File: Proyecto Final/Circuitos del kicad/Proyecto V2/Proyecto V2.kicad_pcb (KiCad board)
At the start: 2 copper layers, 249.8 x 175.1 mm, 40 parts, among them J1 12v, J2 I2C + LCD, J3 DS1307, J4 Encoder, J5 Conn_01x02, J6 Conn_01x02, J7 Conn_01x02, J8 Conn_01x05, J9 Conn_01x05, K1 RAYEX-L90, K2 RAYEX-L90, K3 RAYEX-L90, Q1 PN2222A, Q2 PN2222A, Q3 PN2222A, SW1 SW_Push, SW2 SW_Push, SW3 SW_Push, SW4 SW_Push, U1 LM7805, U3 ATmega328P-P, U4 NodeMCU1.0(ESP-12E), Y1 16MHz

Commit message: SEXOOO
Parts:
- removed J9: Conn_01x05, Connector_PinHeader_2.54mm:PinHeader_1x05_P2.54mm_Vertical
- J4: value Encoder -> Conn_02x06_Odd_Even; footprint Connector_PinSocket_2.54mm:PinSocket_1x05_P2.54mm_Vertical -> Connector_PinHeader_2.54mm:PinHeader_2x06_P2.54mm_Vertical; moved to B.Cu
- moved J4 21.3 mm to (70.3, 44.4)
- moved C2 17.3 mm to (35.6, 64.7)
- moved RELAY1 17.3 mm to (66.6, 79.0)
- moved C1 17.3 mm to (35.6, 47.1)
- moved C3 17.3 mm to (56.6, 81.7)
- moved C4 17.3 mm to (41.5, 81.6)
- moved DS18B20 17.3 mm to (55.3, 70.6)
- moved J1 17.3 mm to (46.5, 88.3)
- moved J2 17.3 mm to (66.5, 30.3)
- moved J3 17.3 mm to (61.7, 30.3)
- moved Lvl_sens1 17.3 mm to (56.9, 43.7)
- moved R1 17.3 mm to (60.4, 66.7)
- moved U1 17.3 mm to (51.6, 75.9)
- moved U3 17.3 mm to (45.2, 33.6)
- moved Y1 17.3 mm to (38.4, 53.4)
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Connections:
- J4 pad 1: Net-(J4-Pad1) -> +5V
- J4 pad 2: Net-(J4-Pad2) -> +5V
- J4 pad 3: unconnected-(J4-Pad3) -> Net-(U3-Pad4)
- J4 pad 4: +5V -> Net-(J4-Pad4)
- J4 pad 5: GND -> Net-(U3-Pad5)
- U3 pad 23: Net-(J4-Pad1) -> Net-(J4-Pad8)
- U3 pad 24: Net-(J4-Pad2) -> Net-(J4-Pad6)
- U3 pad 25: unconnected-(U3-Pad25) -> Net-(J4-Pad4)
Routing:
- net Net-(U3-Pad11): track 31.9 -> 136.1 mm
- net Net-(U3-Pad6): track 17.0 -> 99.6 mm
- net Net-(U3-Pad5): track 16.1 -> 87.8 mm
- net Net-(U3-Pad4): track 16.1 -> 77.3 mm
- net +12V: track 424.7 -> 399.3 mm
- net Net-(J4-Pad4): track 0.00 -> 18.0 mm
- net Net-(J4-Pad6): track 0.00 -> 17.8 mm
- net Net-(J4-Pad8): track 0.00 -> 17.6 mm
- net +5V: track 182.4 -> 165.7 mm
- net Net-(D3-Pad2): track 41.8 -> 30.5 mm
- net Net-(J4-Pad2): track 11.1 -> 0.00 mm
- net Net-(J4-Pad1): track 11.1 -> 0.00 mm
- net Net-(D2-Pad2): track 39.1 -> 34.2 mm
- net GND: track 445.5 -> 441.8 mm
- net Net-(D1-Pad2): track 48.9 -> 52.0 mm
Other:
- board size 249.8 x 175.1 mm -> 239.5 x 178.8 mm

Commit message: Resistencias pullup para pulsadores
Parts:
- removed J8: Conn_01x05, Connector_PinHeader_2.54mm:PinHeader_1x05_P2.54mm_Vertical
- added Encoder/puls1: Conn_02x06_Odd_Even, Connector_PinHeader_2.54mm:PinHeader_2x06_P2.54mm_Vertical, F.Cu at (223.7, 47.6)
- added Encoder1: Conn_01x05, Connector_PinSocket_2.54mm:PinSocket_1x05_P2.54mm_Vertical, F.Cu at (212.9, 19.8)
- added R5: 10k, Resistor_THT:R_Axial_DIN0204_L3.6mm_D1.6mm_P5.08mm_Horizontal, F.Cu at (222.0, 31.8)
- added R6: 10k, Resistor_THT:R_Axial_DIN0204_L3.6mm_D1.6mm_P5.08mm_Horizontal, F.Cu at (218.9, 31.8)
- added R7: 10k, Resistor_THT:R_Axial_DIN0204_L3.6mm_D1.6mm_P5.08mm_Horizontal, F.Cu at (216.0, 31.8)
- added R8: 10k, Resistor_THT:R_Axial_DIN0204_L3.6mm_D1.6mm_P5.08mm_Horizontal, F.Cu at (212.8, 31.8)
- moved SW1 42.1 mm to (174.0, 21.7), turned to 0 degrees
- moved SW2 37.3 mm to (192.4, 21.7), turned to 0 degrees
- moved SW3 14.9 mm to (230.8, 21.8), turned to 0 degrees
- moved SW4 12.1 mm to (248.7, 21.8), turned to 0 degrees
- renumbered ESP2866 to ESP2866-arduino1, U4 to ESP8266, J4 to Encoder/puls-arduino1, K1 to Relay-1, K3 to Relay-2, K2 to Relay-3, J5 to Salida-1, J7 to Salida-2, J6 to Salida-3
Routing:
- net +5V: track 165.7 -> 370.6 mm
- net Net-(Encoder/puls1-Pad4): track 0.00 -> 131.7 mm
- net Net-(Encoder/puls1-Pad6): track 0.00 -> 121.8 mm
- net Net-(Encoder/puls1-Pad8): track 0.00 -> 111.7 mm
- net GND: track 441.8 -> 486.6 mm
- net Net-(Encoder/puls1-Pad9): track 30.4 -> 46.5 mm
- net Net-(Encoder/puls1-Pad3): track 33.8 -> 46.1 mm
- net Net-(Encoder/puls-arduino1-Pad9): track 136.1 -> 126.6 mm
- net Net-(Encoder/puls1-Pad7): track 25.2 -> 33.2 mm
- net Net-(U3-Pad6): track 99.6 -> 92.4 mm
- net Net-(Encoder/puls-arduino1-Pad5): track 87.8 -> 83.6 mm
- net Net-(Encoder/puls1-Pad5): track 29.4 -> 32.0 mm
- net Net-(Encoder/puls-arduino1-Pad3): track 77.3 -> 75.7 mm
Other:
- board size 239.5 x 178.8 mm -> 238.9 x 178.8 mm

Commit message: Cambio GND
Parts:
- moved SW1 14.2 mm to (159.8, 21.7)
- moved SW2 14.2 mm to (178.2, 21.7)
- moved SW4 13.0 mm to (261.7, 21.8)
- moved SW3 13.0 mm to (243.8, 21.8)
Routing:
- net GND: track 486.6 -> 3.69 mm
- net Net-(Encoder/puls1-Pad4): track 131.7 -> 165.2 mm
- net Net-(Encoder/puls1-Pad6): track 121.8 -> 155.1 mm
- net Net-(Encoder/puls1-Pad8): track 111.7 -> 144.6 mm
- net +5V: track 370.6 -> 401.5 mm
- net Net-(Encoder/puls1-Pad5): track 32.0 -> 45.0 mm
- net Net-(Encoder/puls1-Pad7): track 33.2 -> 46.2 mm
- net Net-(Encoder/puls1-Pad9): track 46.5 -> 59.4 mm
- net Net-(Encoder/puls1-Pad3): track 46.1 -> 58.4 mm
- net Net-(Encoder/puls-arduino1-Pad9): track 126.6 -> 127.8 mm
- net Net-(U3-Pad6): track 92.4 -> 93.2 mm
- net Net-(RELAY1-Pad4): track 23.7 -> 23.1 mm
- added copper zone on B.Cu, net GND
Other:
- board size 238.9 x 178.8 mm -> 252.7 x 178.8 mm

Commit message: Detalles menores
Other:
- board size 252.7 x 178.8 mm -> 252.9 x 178.9 mm
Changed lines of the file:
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@@
     (fp_line (start -3.2 9.01) (end 14.48 9.01) (layer "F.SilkS") (width 0.12))
     (fp_line (start 4.064 -5.1054) (end 5.334 -5.1054) (layer "F.SilkS") (width 0.12))
-    (fp_arc (start 5.842266 0.761644) (mid 4.699001 0.381219) (end 5.842001 -0.000002) (layer "F.SilkS") (width 0.12))
+    (fp_arc (start 5.842266 0.761644) (mid 4.699001 0.381223) (end 5.842001 -0.000002) (layer "F.SilkS") (width 0.12))
     (fp_arc (start 10.13 -12.44) (mid 10.384817 -13.055183) (end 11 -13.31) (layer "F.SilkS") (width 0.12))
     (fp_arc (start 5.8418 -0.761733) (mid 4.765964 -0.859168) (end 5.334 -1.778) (layer "F.SilkS") (width 0.12))
@@
     (fp_arc (start 16 14.31) (mid 15.384817 14.055183) (end 15.13 13.44) (layer "F.SilkS") (width 0.12))
     (fp_arc (start 27.08 -13.31) (mid 27.695183 -13.055183) (end 27.95 -12.44) (layer "F.SilkS") (width 0.12))
-    (fp_arc (start 5.334002 1.777997) (mid 4.765969 0.859167) (end 5.841802 0.76173) (layer "F.SilkS") (width 0.12))
-    (fp_arc (start 5.842265 -0.000355) (mid 4.699 -0.38078) (end 5.842 -0.762001) (layer "F.SilkS") (width 0.12))
+    (fp_arc (start 5.334002 1.777997) (mid 4.765966 0.859171) (end 5.841802 0.76173) (layer "F.SilkS") (width 0.12))
+    (fp_arc (start 5.842265 -0.000355) (mid 4.699001 -0.380778) (end 5.842 -0.762001) (layer "F.SilkS") (width 0.12))
     (fp_arc (start 27.95 13.44) (mid 27.695183 14.055183) (end 27.08 14.31) (layer "F.SilkS") (width 0.12))
     (fp_circle (center 21.59 -2.54) (end 21.59 -2.413) (layer "F.SilkS") (width 0.12) (fill none))
@@
     (fp_line (start 17.74 6.604) (end 17.74 1.778) (layer "F.SilkS") (width 0.12))
     (fp_arc (start 5.8418 -0.761733) (mid 4.765964 -0.859168) (end 5.334 -1.778) (layer "F.SilkS") (width 0.12))
-    (fp_arc (start 5.842265 -0.000355) (mid 4.699 -0.38078) (end 5.842 -0.762001) (layer "F.SilkS") (width 0.12))
-    (fp_arc (start 5.842266 0.761644) (mid 4.699001 0.381219) (end 5.842001 -0.000002) (layer "F.SilkS") (width 0.12))
+    (fp_arc (start 5.842265 -0.000355) (mid 4.699001 -0.380778) (end 5.842 -0.762001) (layer "F.SilkS") (width 0.12))
+    (fp_arc (start 5.842266 0.761644) (mid 4.699001 0.381223) (end 5.842001 -0.000002) (layer "F.SilkS") (width 0.12))
     (fp_arc (start 27.08 -13.31) (mid 27.695183 -13.055183) (end 27.95 -12.44) (layer "F.SilkS") (width 0.12))
     (fp_arc (start 16 14.31) (mid 15.384817 14.055183) (end 15.13 13.44) (layer "F.SilkS") (width 0.12))
@@
     (fp_arc (start -4.07 -9.94) (mid -3.815183 -10.555183) (end -3.2 -10.81) (layer "F.SilkS") (width 0.12))
     (fp_arc (start 10.13 -11.46) (mid 9.939619 -11.000381) (end 9.48 -10.81) (layer "F.SilkS") (width 0.12))
-    (fp_arc (start 5.334002 1.777997) (mid 4.765969 0.859167) (end 5.841802 0.76173) (layer "F.SilkS") (width 0.12))
+    (fp_arc (start 5.334002 1.777997) (mid 4.765966 0.859171) (end 5.841802 0.76173) (layer "F.SilkS") (width 0.12))
     (fp_arc (start -3.2 9.01) (mid -3.815183 8.755183) (end -4.07 8.14) (layer "F.SilkS") (width 0.12))
     (fp_arc (start 10.13 -12.44) (mid 10.384817 -13.055183) (end 11 -13.31) (layer "F.SilkS") (width 0.12))
@@
     (fp_arc (start 5.8418 -0.761733) (mid 4.765964 -0.859168) (end 5.334 -1.778) (layer "F.SilkS") (width 0.12))
     (fp_arc (start 10.13 -12.44) (mid 10.384817 -13.055183) (end 11 -13.31) (layer "F.SilkS") (width 0.12))
-    (fp_arc (start 5.334002 1.777997) (mid 4.765969 0.859167) (end 5.841802 0.76173) (layer "F.SilkS") (width 0.12))
+    (fp_arc (start 5.334002 1.777997) (mid 4.765966 0.859171) (end 5.841802 0.76173) (layer "F.SilkS") (width 0.12))
     (fp_arc (start 27.95 13.44) (mid 27.695183 14.055183) (end 27.08 14.31) (layer "F.SilkS") (width 0.12))
-    (fp_arc (start 5.842265 -0.000355) (mid 4.699 -0.38078) (end 5.842 -0.762001) (layer "F.SilkS") (width 0.12))
-    (fp_arc (start 5.842266 0.761644) (mid 4.699001 0.381219) (end 5.842001 -0.000002) (layer "F.SilkS") (width 0.12))
+    (fp_arc (start 5.842265 -0.000355) (mid 4.699001 -0.380778) (end 5.842 -0.762001) (layer "F.SilkS") (width 0.12))
+    (fp_arc (start 5.842266 0.761644) (mid 4.699001 0.381223) (end 5.842001 -0.000002) (layer "F.SilkS") (width 0.12))
     (fp_arc (start 10.13 -11.46) (mid 9.939619 -11.000381) (end 9.48 -10.81) (layer "F.SilkS") (width 0.12))
     (fp_arc (start -3.2 9.01) (mid -3.815183 8.755183) (end -4.07 8.14) (layer "F.SilkS") (width 0.12))
@@
     )
   )
-  (gr_rect (start 153.39 15.162161) (end 278.428479 56.21358) (layer "Edge.Cuts") (width 0.2) (fill none))
-  (gr_rect (start 114.61 14.4) (end 147.2 81.86) (layer "Edge.Cuts") (width 0.2) (fill none))
-  (gr_rect (start 77.035 23.33) (end 32.775 93.14) (layer "Edge.Cuts") (width 0.2) (fill none))
-  (gr_rect (start 25.74 105) (end 134.26 193.24) (layer "Edge.Cuts") (width 0.2) (fill none))
+  (gr_rect (start 153.28 15.152161) (end 278.518479 56.30358) (layer "Edge.Cuts") (width 0.2) (fill none))
+  (gr_rect (start 114.58 14.32) (end 147.24 81.93) (layer "Edge.Cuts") (width 0.2) (fill none))
+  (gr_rect (start 77.125 23.33) (end 32.775 93.14) (layer "Edge.Cuts") (width 0.2) (fill none))
+  (gr_rect (start 25.64 104.91) (end 134.35 193.24) (layer "Edge.Cuts") (width 0.2) (fill none))
   (dimension (type aligned) (layer "B.Cu")
     (pts (xy 77.225 23.36) (xy 77.225 93.16))
     (height -4.835)
-    (gr_text "69,8000 mm" (at 81.26 58.53 90) (layer "B.Cu")
+    (gr_text "69.8000 mm" (at 81.26 58.53 90) (layer "B.Cu")
       (effects (font (size 1.5 1.5) (thickness 0.3)))
     )
@@
   )
   (dimension (type aligned) (layer "B.Cu")
-    (pts (xy 32.775 93.14) (xy 77.035 93.14))
+    (pts (xy 32.775 93.14) (xy 77.125 93.14))
     (height 3.47)
-    (gr_text "44,2600 mm" (at 54.94 96.43) (layer "B.Cu")
+    (gr_text "44.3500 mm" (at 54.94 96.43) (layer "B.Cu")
       (effects (font (size 1.5 1.5) (thickness 0.3)))
     )
@@
       (pts
         (xy 134.15 193.13)
-        (xy 25.9 193.1)
+        (xy 25.85 193.13)
         (xy 25.85 105.11)
-        (xy 134.1 105.2)
+        (xy 134.15 105.11)
       )
     )

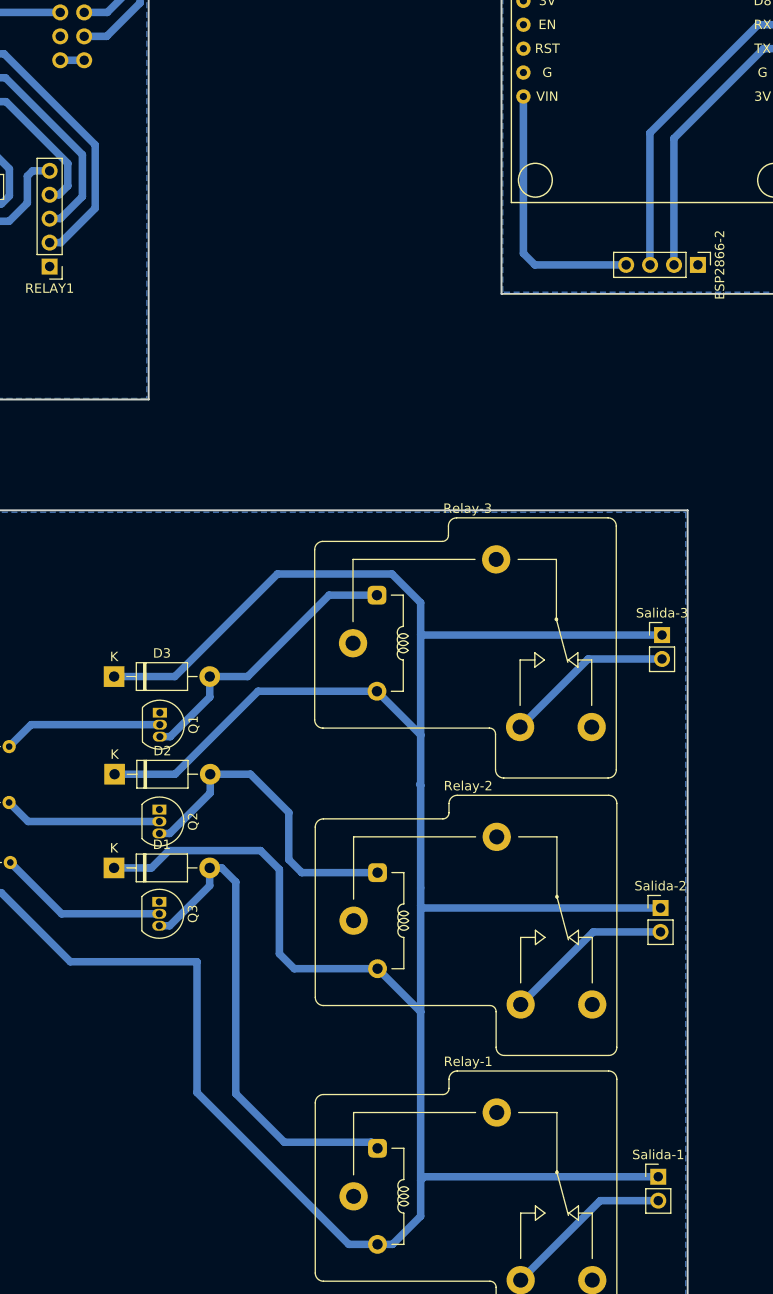
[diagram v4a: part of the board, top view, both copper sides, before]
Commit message: cambio bornera
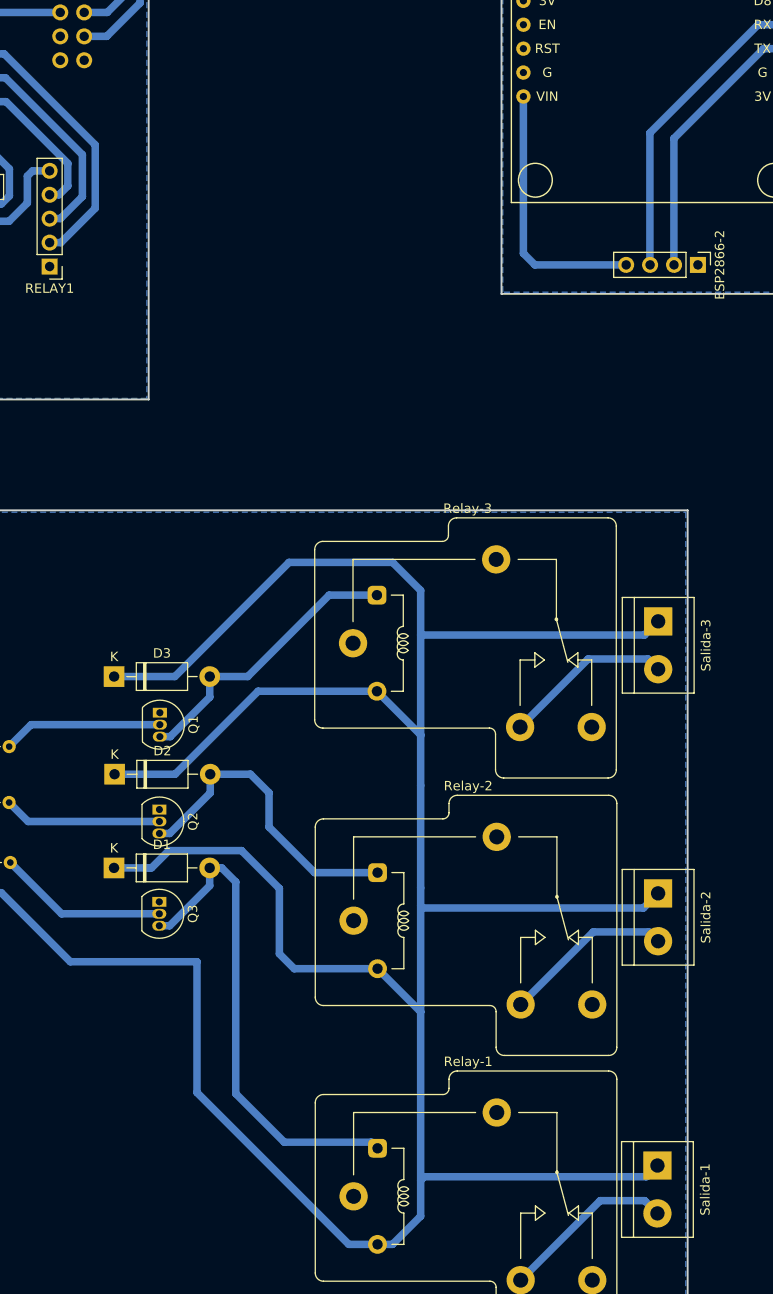
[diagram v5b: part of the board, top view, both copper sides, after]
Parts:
- Salida-1, Salida-2, Salida-3: footprint Connector_PinHeader_2.54mm:PinHeader_1x02_P2.54mm_Vertical -> TerminalBlock:TerminalBlock_bornier-2_P5.08mm
- moved Salida-2 1.58 mm to (131.2, 145.6), turned to -90 degrees
- moved Salida-3 1.51 mm to (131.2, 116.7), turned to -90 degrees
- moved Salida-1 1.19 mm to (131.1, 174.5), turned to -90 degrees
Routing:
- net GND: track 3.69 -> 1.15 mm
- net +12V: track 399.6 -> 401.0 mm
- net Net-(D2-Pad2): track 34.2 -> 33.4 mm
